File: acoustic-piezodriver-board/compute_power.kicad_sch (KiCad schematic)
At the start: 29 parts, among them J301 Conn_02x06_Odd_Even, U10 NCE6005AS, U302 TMCS1108A3UQDR, U9 LM3478MM

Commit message: [production checks] checked caps, [todo] Think about replacing 220 nF filtering caps in DC-DC to 0402 package (next) check rest of footprints
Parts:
- C32: footprint Capacitor_SMD:C_0603_1608Metric -> Capacitor_SMD:C_0805_2012Metric; LPN (none) -> C5378; MPN (none) -> CL21B224KBFNNNE
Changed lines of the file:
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@@
 			)
 		)
-		(property "Footprint" "Capacitor_SMD:C_0603_1608Metric"
+		(property "Footprint" "Capacitor_SMD:C_0805_2012Metric"
 			(at 182.88 99.06 0)
 			(effects
@@
 			(effects
 				(font
+					(size 1.27 1.27)
+				)
+				(hide yes)
+			)
+		)
+		(property "LPN" "C5378"
+			(at 182.88 99.06 90)
+			(effects
+				(font
+					(size 1.27 1.27)
+				)
+				(hide yes)
+			)
+		)
+		(property "MPN" "CL21B224KBFNNNE"
+			(at 182.88 99.06 90)
+			(effects
+				(font

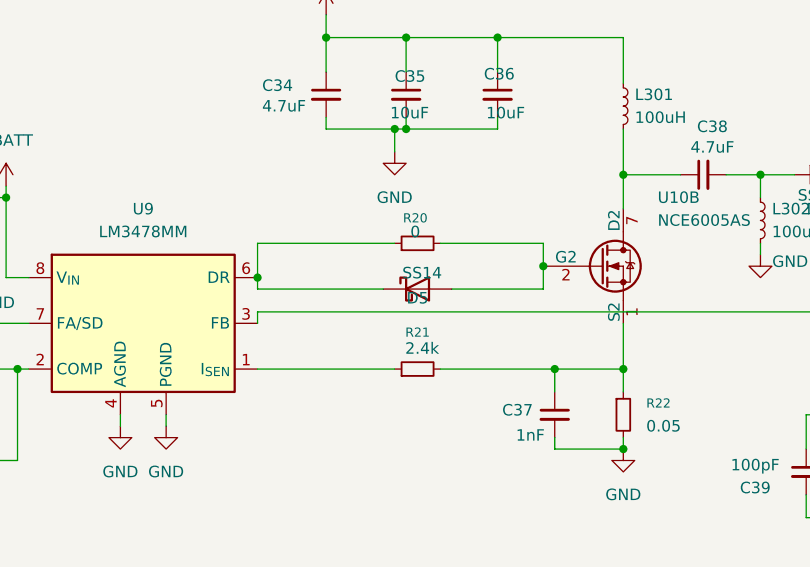
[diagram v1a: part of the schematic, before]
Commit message: changed ss520 footprints
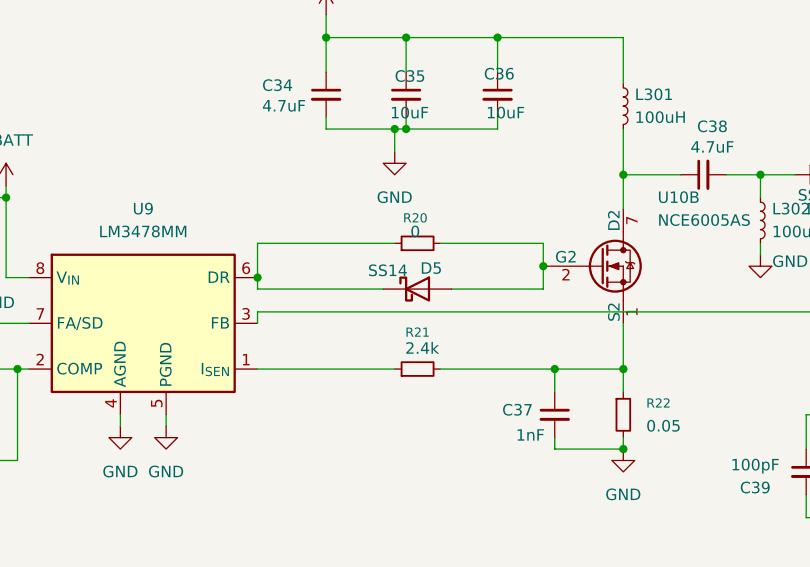
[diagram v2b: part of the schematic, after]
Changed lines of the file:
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@@
 		(dnp no)
 		(property "Reference" "D5"
-			(at 242.57 91.186 0)
+			(at 244.094 87.884 0)
 			(effects
 				(font
@@
 		)
 		(property "Value" "SS14"
-			(at 243.078 88.392 0)
+			(at 239.268 88.138 0)
 			(effects
 				(font
@@
 			)
 		)
-		(property "Description" "Vf 0.55, If 5A"
+		(property "Description" "Vf 0.55, If 5A, DCblock 20 V"
 			(at 287.02 77.47 0)
 			(effects

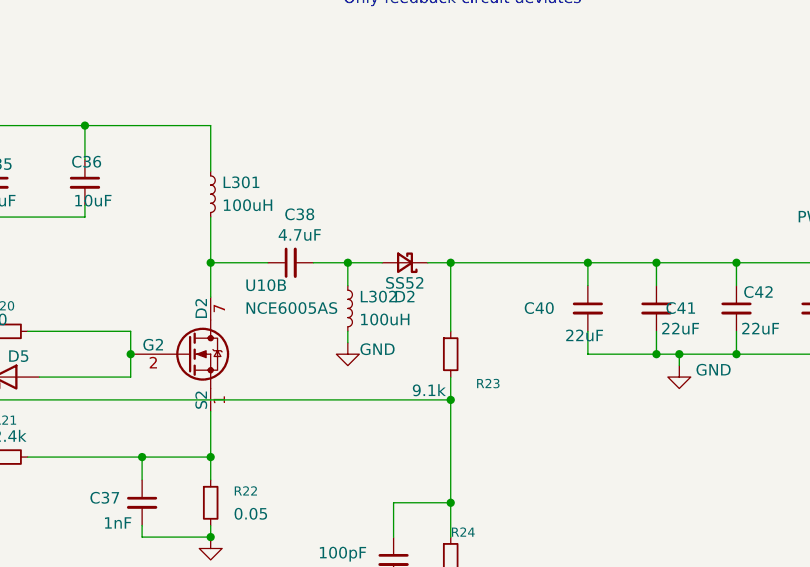
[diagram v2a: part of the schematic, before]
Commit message: checked components until mosfets
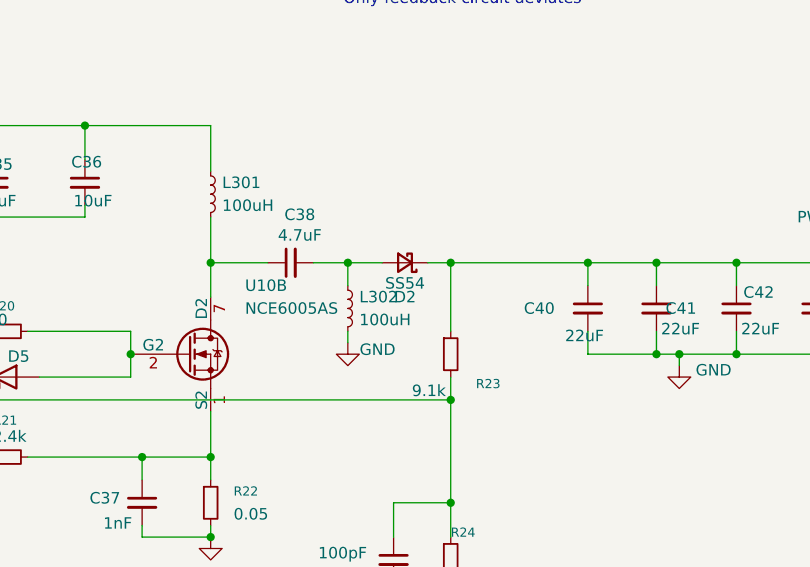
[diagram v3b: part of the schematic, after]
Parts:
- D2: value SS52 -> SS54; footprint Diode_SMD:D_SMA-SMB_Universal_Handsoldering -> Diode_SMD:D_SMA
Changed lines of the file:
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@@
 			)
 		)
-		(property "Value" "SS52"
+		(property "Value" "SS54"
 			(at 287.02 79.756 0)
 			(effects
@@
 			)
 		)
-		(property "Footprint" "Diode_SMD:D_SMA-SMB_Universal_Handsoldering"
+		(property "Footprint" "Diode_SMD:D_SMA"
 			(at 287.02 77.47 90)
 			(effects

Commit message: completed footprint check (next) reroute pbootstrap circuit on top layer only, fix errors after footprint change
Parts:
- U10: footprint Package_SO:SOP-8-1EP_4.57x4.57mm_P1.27mm_EP4.57x4.45mm_ThermalVias -> Package_SO:SOIC-8_3.9x4.9mm_P1.27mm
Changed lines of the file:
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@@
 			)
 		)
-		(property "Footprint" "Package_SO:SOP-8-1EP_4.57x4.57mm_P1.27mm_EP4.57x4.45mm_ThermalVias"
+		(property "Footprint" "Package_SO:SOIC-8_3.9x4.9mm_P1.27mm"
 			(at 269.24 87.63 0)
 			(effects
@@
 			)
 		)
-		(property "Footprint" "Package_SO:SOP-8-1EP_4.57x4.57mm_P1.27mm_EP4.57x4.45mm_ThermalVias"
+		(property "Footprint" "Package_SO:SOIC-8_3.9x4.9mm_P1.27mm"
 			(at 328.93 134.62 0)
 			(effects

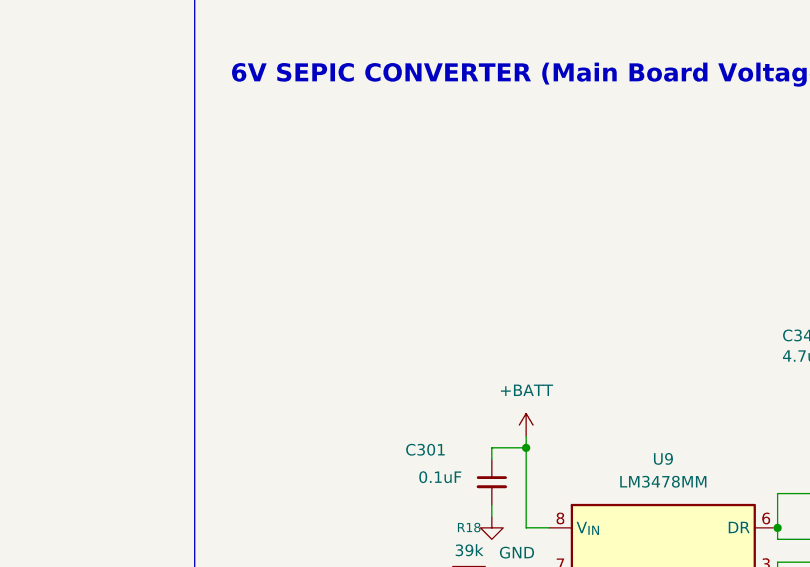
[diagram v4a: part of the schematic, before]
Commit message: fixed erc and drc errors completely, added 3d models for connectors, finished DFM (next) create gerbers, check
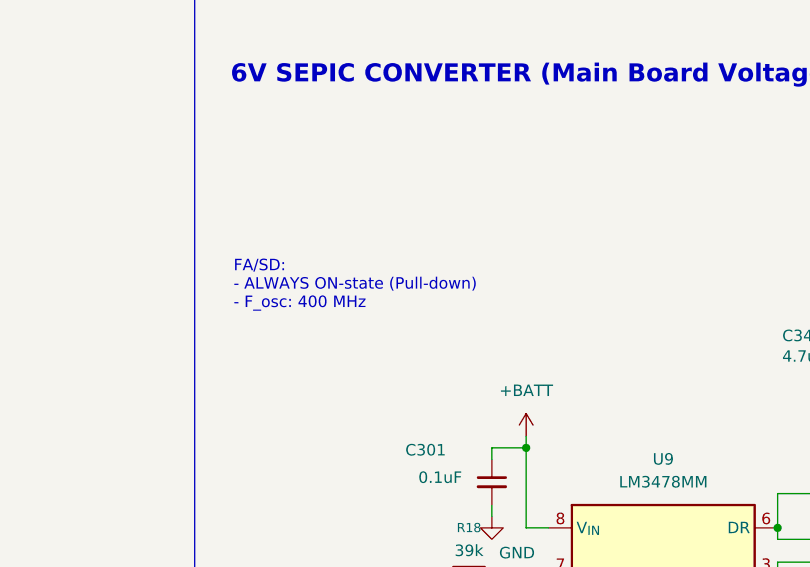
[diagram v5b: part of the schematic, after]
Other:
- note added: "FA/SD: - ALWAYS ON-state (Pull-down) - F_osc: 400 MHz"
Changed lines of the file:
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@@
+		)
+	)
+	(text "FA/SD: \n- ALWAYS ON-state (Pull-down)\n- F_osc: 400 MHz"
+		(exclude_from_sim no)
+		(at 164.338 61.976 0)
+		(effects
+			(font
+				(size 1.27 1.27)
+			)
+			(justify left)
 		)
 	)

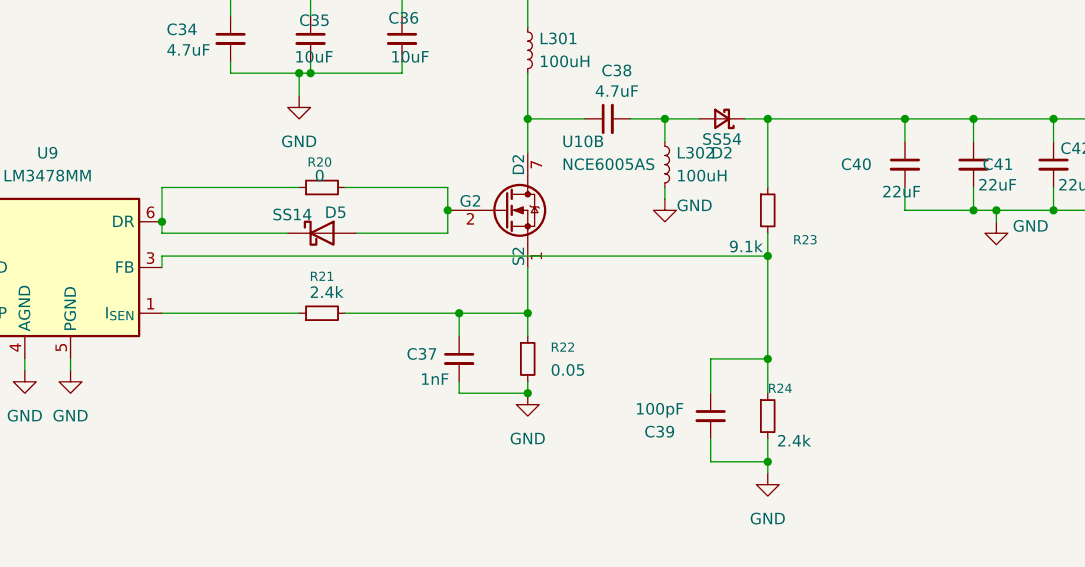
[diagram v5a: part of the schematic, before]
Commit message: added testpoints on fb and isense pins (next) double-check schematic and order
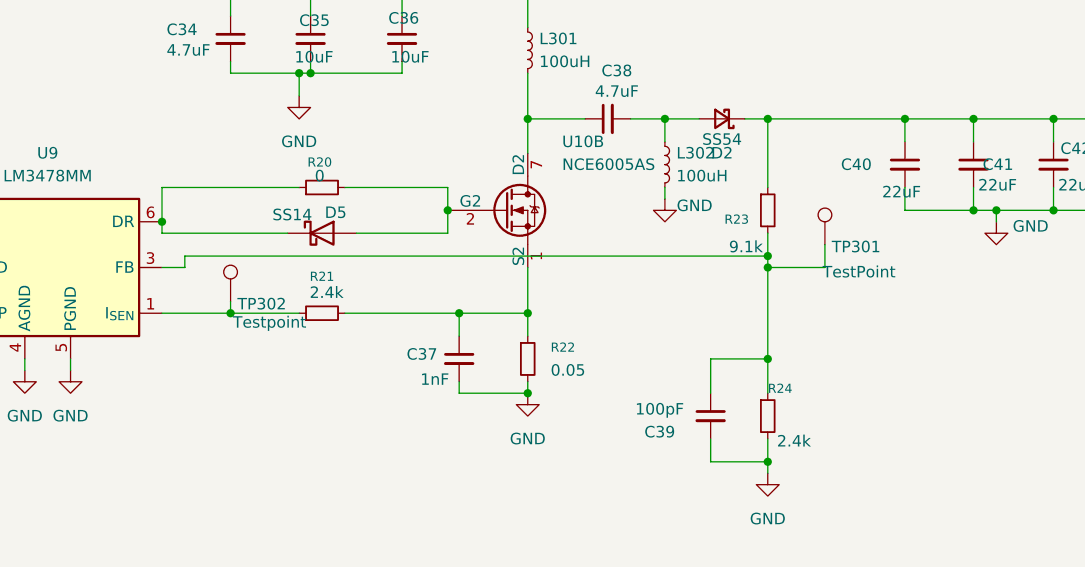
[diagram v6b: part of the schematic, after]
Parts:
- added TP301: TestPoint, TestPoint:TestPoint_Pad_D1.0mm, symbol iw-misc:TestPoint_0.25mm
- added TP302: Testpoint, TestPoint:TestPoint_Pad_D1.0mm, symbol iw-misc:TestPoint_0.25mm
- C301, C304: LCSC Part Number (none) -> C307331; LPN C307331 -> (none); MPN CL05B104KB54PNC -> (none); Manufacturing Part Number (none) -> CL05B104KB54PNC
- C32: LCSC Part Number (none) -> C5378; LPN C5378 -> (none); MPN CL21B224KBFNNNE -> (none); Manufacturing Part Number (none) -> CL21B224KBFNNNE
- C33: LCSC Part Number (none) -> C1663; LPN C1663 -> (none); MPN CL10C330JB8NNNC -> (none); Manufacturing Part Number (none) -> CL10C330JB8NNNC
- C34, C38: LCSC Part Number (none) -> C29823; LPN C29823 -> (none); MPN 1206B475K500NT -> (none); Manufacturing Part Number (none) -> 1206B475K500NT
- C35, C36: LCSC Part Number (none) -> C440198; LPN C440198 -> (none); MPN GRM21BR61H106KE43L -> (none); Manufacturing Part Number (none) -> GRM21BR61H106KE43L
- C37: LCSC Part Number (none) -> C1523; LPN C1523 -> (none); MPN 0402B102K500NT -> (none); Manufacturing Part Number (none) -> 0402B102K500NT
- C39: LCSC Part Number (none) -> C1546; LPN C1546 -> (none); MPN 0402CG101J500NT -> (none); Manufacturing Part Number (none) -> 0402CG101J500NT
- C40, C41, C42, C43: LCSC Part Number (none) -> C45783; LPN C45783 -> (none); MPN CL21A226MAQNNNE -> (none); Manufacturing Part Number (none) -> CL21A226MAQNNNE
- D2: LCSC Part Number (none) -> C22452; LPN C22452 -> (none); MPN SS54 -> (none); Manufacturing Part Number (none) -> SS54
- D5: LCSC Part Number (none) -> C2480; LPN C2480 -> (none); MPN SS14 -> (none); Manufacturing Part Number (none) -> SS14
- J301: LCSC Part Number (none) -> C124388; LPN C124388 -> (none); MPN B-2100S12P-B110 -> (none); Manufacturing Part Number (none) -> B-2100S12P-B110
- L301, L302: LCSC Part Number (none) -> C5273830; LPN C5273830 -> (none); MPN PSPMAA1050H-101M-ANP -> (none); Manufacturing Part Number (none) -> PSPMAA1050H-101M-ANP
- R18: LCSC Part Number (none) -> C23153; LPN C23153 -> (none); MPN 0603WAF3902T5E -> (none); Manufacturing Part Number (none) -> 0603WAF3902T5E
- R19: LCSC Part Number (none) -> C13167; LPN C13167 -> (none); MPN 0603WAF2701T5E -> (none); Manufacturing Part Number (none) -> 0603WAF2701T5E
- R20: LCSC Part Number (none) -> C15402; LPN C15402 -> (none); MPN 0603WAJ0000T5E -> (none); Manufacturing Part Number (none) -> 0603WAJ0000T5E
- R21: LCSC Part Number (none) -> C17526; LPN C17526 -> (none); MPN 0805W8F2401T5E -> (none); Manufacturing Part Number (none) -> 0805W8F2401T5E
- R22: LCSC Part Number (none) -> C127691; LPN C127691 -> (none); MPN 1206W3F500MT5E -> (none); Manufacturing Part Number (none) -> 1206W3F500MT5E
- R23: LCSC Part Number (none) -> C23260; LPN C23260 -> (none); MPN 0603WAF9101T5E -> (none); Manufacturing Part Number (none) -> 0603WAF9101T5E
- R24: LCSC Part Number (none) -> C22940; LPN C22940 -> (none); MPN 0603WAF2401T5E -> (none); Manufacturing Part Number (none) -> 0603WAF2401T5E
- U10: LCSC Part Number (none) -> C126151; LPN C126151 -> (none); MPN NCE6005AS -> (none); Manufacturing Part Number (none) -> NCE6005AS
- U302: LCSC Part Number (none) -> C3684263; LPN C3684263 -> (none); MPN TMCS1108A3UQDR -> (none); Manufacturing Part Number (none) -> TMCS1108A3UQDR
- U9: LCSC Part Number (none) -> C404045; LPN C404045 -> (none); MPN LM3478MMX/NOPB -> (none); Manufacturing Part Number (none) -> LM3478MMX/NOPB
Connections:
- net at C39.1, R23.2, R24.1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: now also TP301.1
- net at R21.1, U9.1 (I_{SEN}): now also TP302.1

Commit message: added gerbers
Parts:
- TP301, TP302: now left out of the parts list
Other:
- note added: "DC-DC (SEPIC) VBAT -> 5.5 V (dimensioned for 6 V) Only feedback circuit deviates RDIV: - 6 V * (2.4 / (2.4 + 9.1))) = 1.25 V"
- note removed: "DC-DC (SEPIC) VBAT -> 5.5 V (dimensioned for 6 V) Only feedback circuit deviates"
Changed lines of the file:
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@@
 		)
 	)
-	(text "DC-DC (SEPIC) VBAT -> 5.5 V (dimensioned for 6 V)\nOnly feedback circuit deviates"
+	(text "DC-DC (SEPIC) VBAT -> 5.5 V (dimensioned for 6 V)\nOnly feedback circuit deviates\nRDIV:\n- 6 V * (2.4 / (2.4 + 9.1))) = 1.25 V"
 		(exclude_from_sim no)
 		(at 280.162 47.244 0)
@@
 		(unit 1)
 		(exclude_from_sim no)
-		(in_bom yes)
+		(in_bom no)
 		(on_board yes)
 		(dnp no)
@@
 		(unit 1)
 		(exclude_from_sim no)
-		(in_bom yes)
+		(in_bom no)
 		(on_board yes)
 		(dnp no)
